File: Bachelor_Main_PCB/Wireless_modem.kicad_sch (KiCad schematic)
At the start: 57 parts, among them J10 JAE_SIM_Card_SF72S006, J12 M20-9990245, J18 CONMHF1-SMD-G-T, J19 CONMHF1-SMD-G-T, J20 CONMHF1-SMD-G-T, Q1 SSM3J358R,LF, Q10 NX3008NBKW, Q11 NX3008NBKW, Q5 NX3008NBKW, Q6 NX3008NBKW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

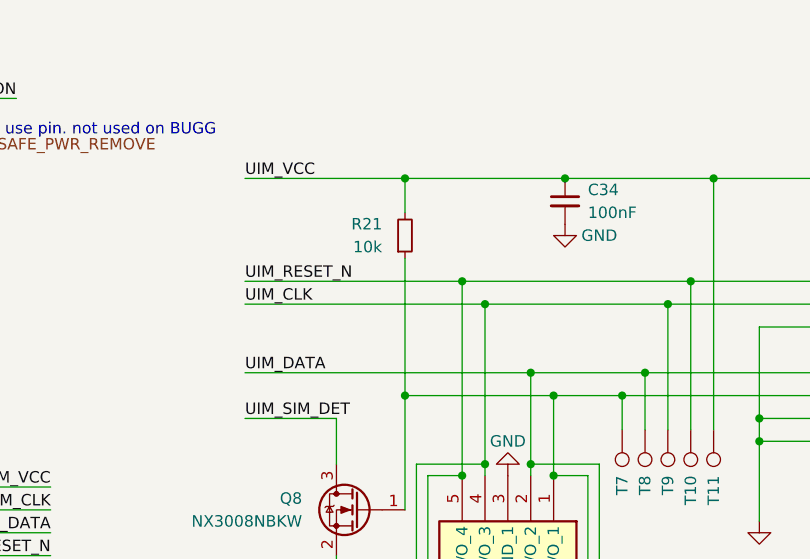
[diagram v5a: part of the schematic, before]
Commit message: add UIM_VCC to UIM_DATA pullout which is DNP
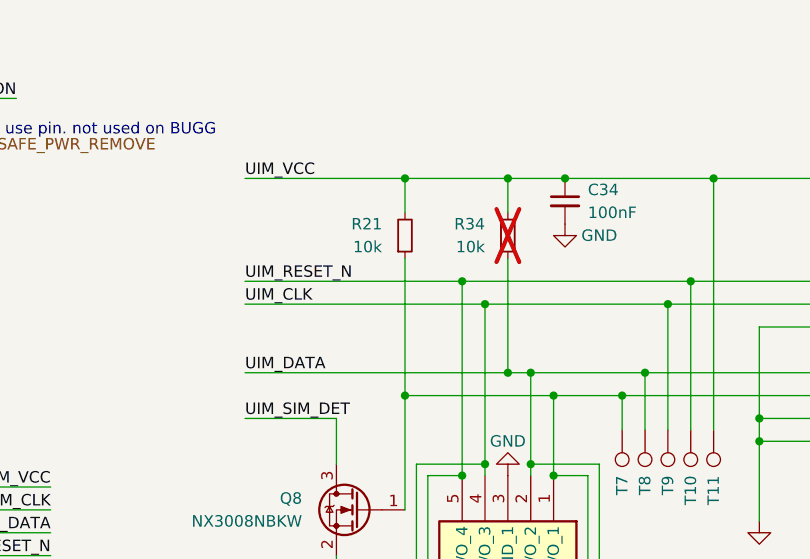
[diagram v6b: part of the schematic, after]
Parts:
- added R34: 10k, Resistor_SMD:R_0402_1005Metric, symbol Device:R_Small
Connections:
- net UIM_DATA: now also R34.1
- net UIM_VCC: now also R34.2
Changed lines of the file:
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@@
 	)
 	(junction
+		(at 209.55 33.02)
+		(diameter 0)
+		(color 0 0 0 0)
+	)
+	(junction
 		(at 38.1 102.87)
 		(diameter 0)
@@
 	)
 	(junction
+		(at 209.55 54.61)
+		(diameter 0)
+		(color 0 0 0 0)
+	)
+	(junction
 		(at 215.9 33.02)
 		(diameter 0)
@@
 	(wire
 		(pts
+			(xy 209.55 33.02) (xy 209.55 36.83)
+		)
+		(stroke
+			(width 0)
+			(type default)
+		)
+	)
+	(wire
+		(pts
 			(xy 128.27 181.61) (xy 135.89 181.61)
 		)
@@
 	(wire
 		(pts
+			(xy 209.55 41.91) (xy 209.55 54.61)
+		)
+		(stroke
+			(width 0)
+			(type default)
+		)
+	)
+	(wire
+		(pts
 			(xy 29.21 105.41) (xy 30.48 105.41)
 		)
@@
 	(wire
 		(pts
+			(xy 209.55 33.02) (xy 215.9 33.02)
+		)
+		(stroke
+			(width 0)
+			(type default)
+		)
+	)
+	(wire
+		(pts
 			(xy 193.04 107.95) (xy 193.04 109.22)
 		)
@@
 	(wire
 		(pts
-			(xy 198.12 33.02) (xy 215.9 33.02)
+			(xy 198.12 33.02) (xy 209.55 33.02)
 		)
 		(stroke
@@
 	(wire
 		(pts
-			(xy 180.34 54.61) (xy 212.09 54.61)
+			(xy 180.34 54.61) (xy 209.55 54.61)
 		)
 		(stroke
@@
 	(wire
 		(pts
+			(xy 209.55 54.61) (xy 212.09 54.61)
+		)
+		(stroke
+			(width 0)
+			(type default)
+		)
+	)
+	(wire
+		(pts
 			(xy 52.07 100.33) (xy 62.23 100.33)
 		)
@@
 					(unit 1)
 				)
+			)
+		)
+	)
+	(symbol
+		(lib_id "Device:R_Small")
+		(at 209.55 39.37 0)
+		(mirror x)
+		(unit 1)
+		(exclude_from_sim no)
+		(in_bom yes)
+		(on_board yes)
+		(dnp yes)
+		(property "Reference" "R34"
+			(at 207.01 38.1 0)
+			(effects
+				(font
+					(size 1.27 1.27)
+				)
+				(justify right)
+			)
+		)
+		(property "Value" "10k"
+			(at 207.01 40.64 0)
+			(effects
+				(font
+					(size 1.27 1.27)
+				)
+				(justify right)
+			)
+		)
+		(property "Footprint" "Resistor_SMD:R_0402_1005Metric"
+			(at 209.55 39.37 0)
+			(effects
+				(font
+					(size 1.27 1.27)
+				)
+				(hide yes)
+			)
+		)
+		(property "Datasheet" "~"
+			(at 209.55 39.37 0)
+			(effects
+				(font
+					(size 1.27 1.27)
+				)
+				(hide yes)
+			)
+		)
+		(property "Description" ""
+			(at 209.55 39.37 0)
+			(effects
+				(font
+					(size 1.27 1.27)
+				)
+				(hide yes)
+			)
+		)
+		(property "Quantity" ""
+			(at 209.55 39.37 0)
+			(effects
+				(font
+					(size 1.27 1.27)
+				)
+				(hide yes)
+			)
+		)
+		(property "Digikey" ""
+			(at 209.55 39.37 0)
+			(effects
+				(font
+					(size 1.27 1.27)
+				)
+				(hide yes)
+			)
+		)
+		(property "MPN" ""
+			(at 209.55 39.37 0)
+			(effects
+				(font
+					(size 1.27 1.27)
+				)
+				(hide yes)
+			)
+		)
+		(property "Mouser" ""
+			(at 209.55 39.37 0)
+			(effects
+				(font
+					(size 1.27 1.27)
+				)
+				(hide yes)
+			)
+		)
+		(property "Farnell" ""
+			(at 209.55 39.37 0)
+			(effects
+				(font
+					(size 1.27 1.27)
+				)
+				(hide yes)
+			)
+		)
+		(property "Field-1" ""
+			(at 209.55 39.37 0)
+			(effects
+				(font
+					(size 1.27 1.27)
+				)
+				(hide yes)
+			)
+		)
+		(property "Field4" ""
+			(at 209.55 39.37 0)
+			(effects
+				(font
+					(size 1.27 1.27)
+				)
+				(hide yes)
+			)
+		)
+		(property "Field5" ""
+			(at 209.55 39.37 0)
+			(effects
+				(font
+					(size 1.27 1.27)
+				)
+				(hide yes)
+			)
+		)
+		(property "MANUFACTURER" ""
+			(at 209.55 39.37 0)
+			(effects
+				(font
+					(size 1.27 1.27)
+				)
+				(hide yes)
+			)
+		)
+		(pin "1"
+		)
+		(pin "2"
+		)
+		(instances
+			(project "Bachelor_Main_PCB"
+				(path "/3544d663-329e-4884-b753-28436ca187e8/0bbef2a3-1d79-4cf0-b531-d6abf690b331"
+					(reference "R34")
+					(unit 1)
+				)

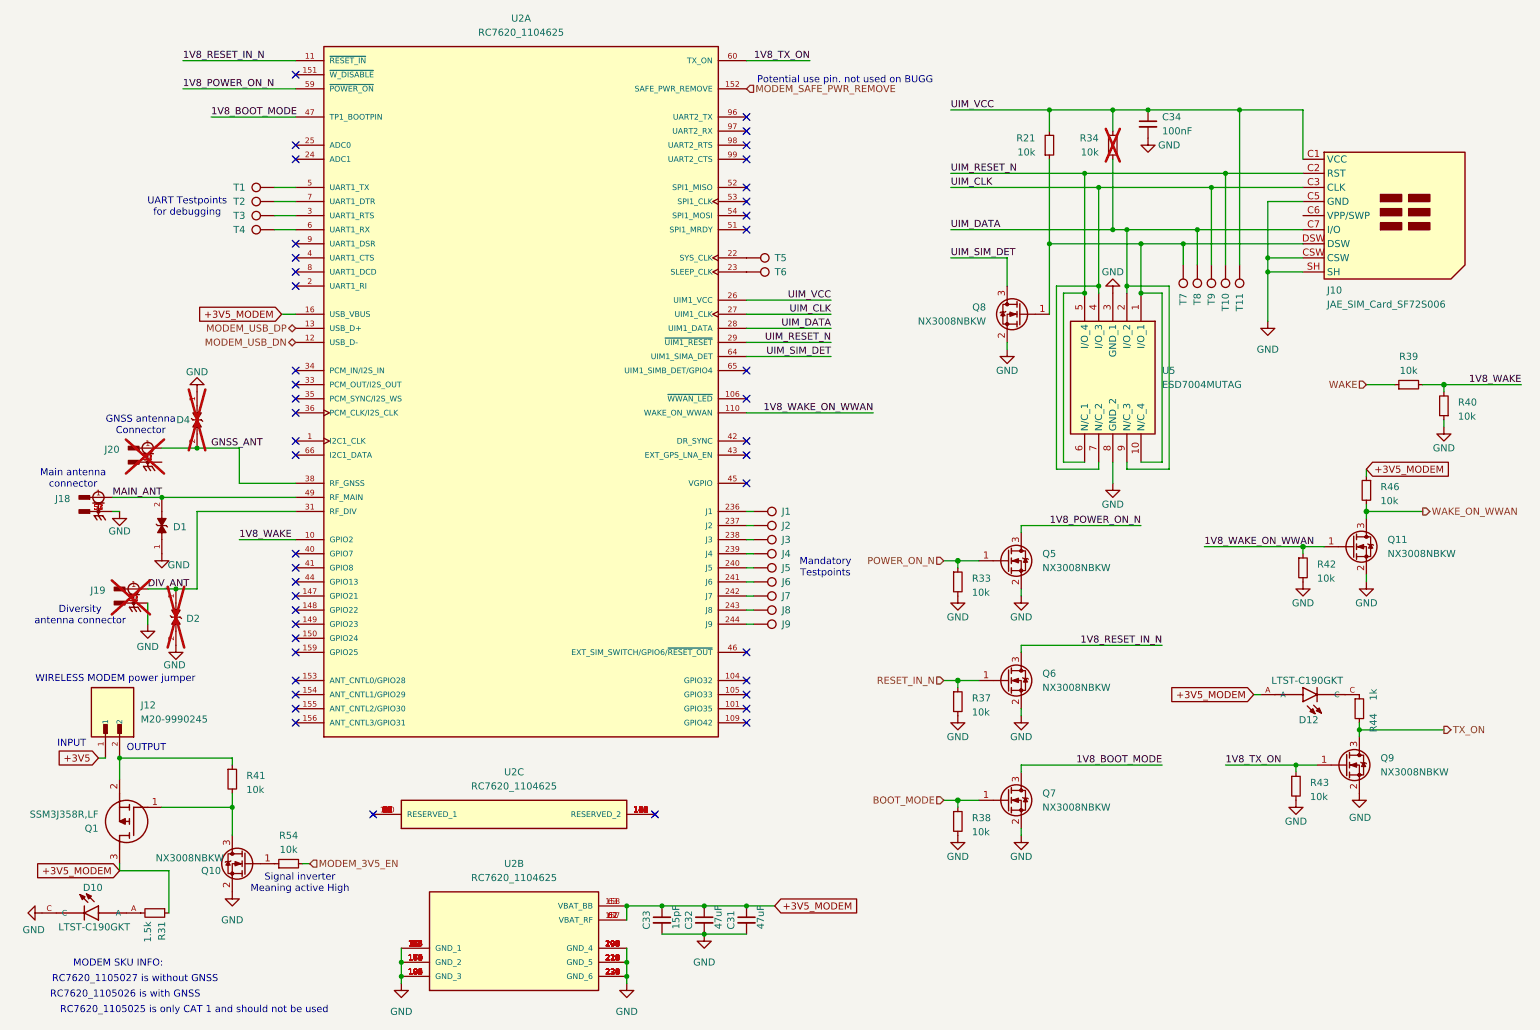
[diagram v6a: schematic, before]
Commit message: Updated the "Part-no" field in the symbol field table for all components
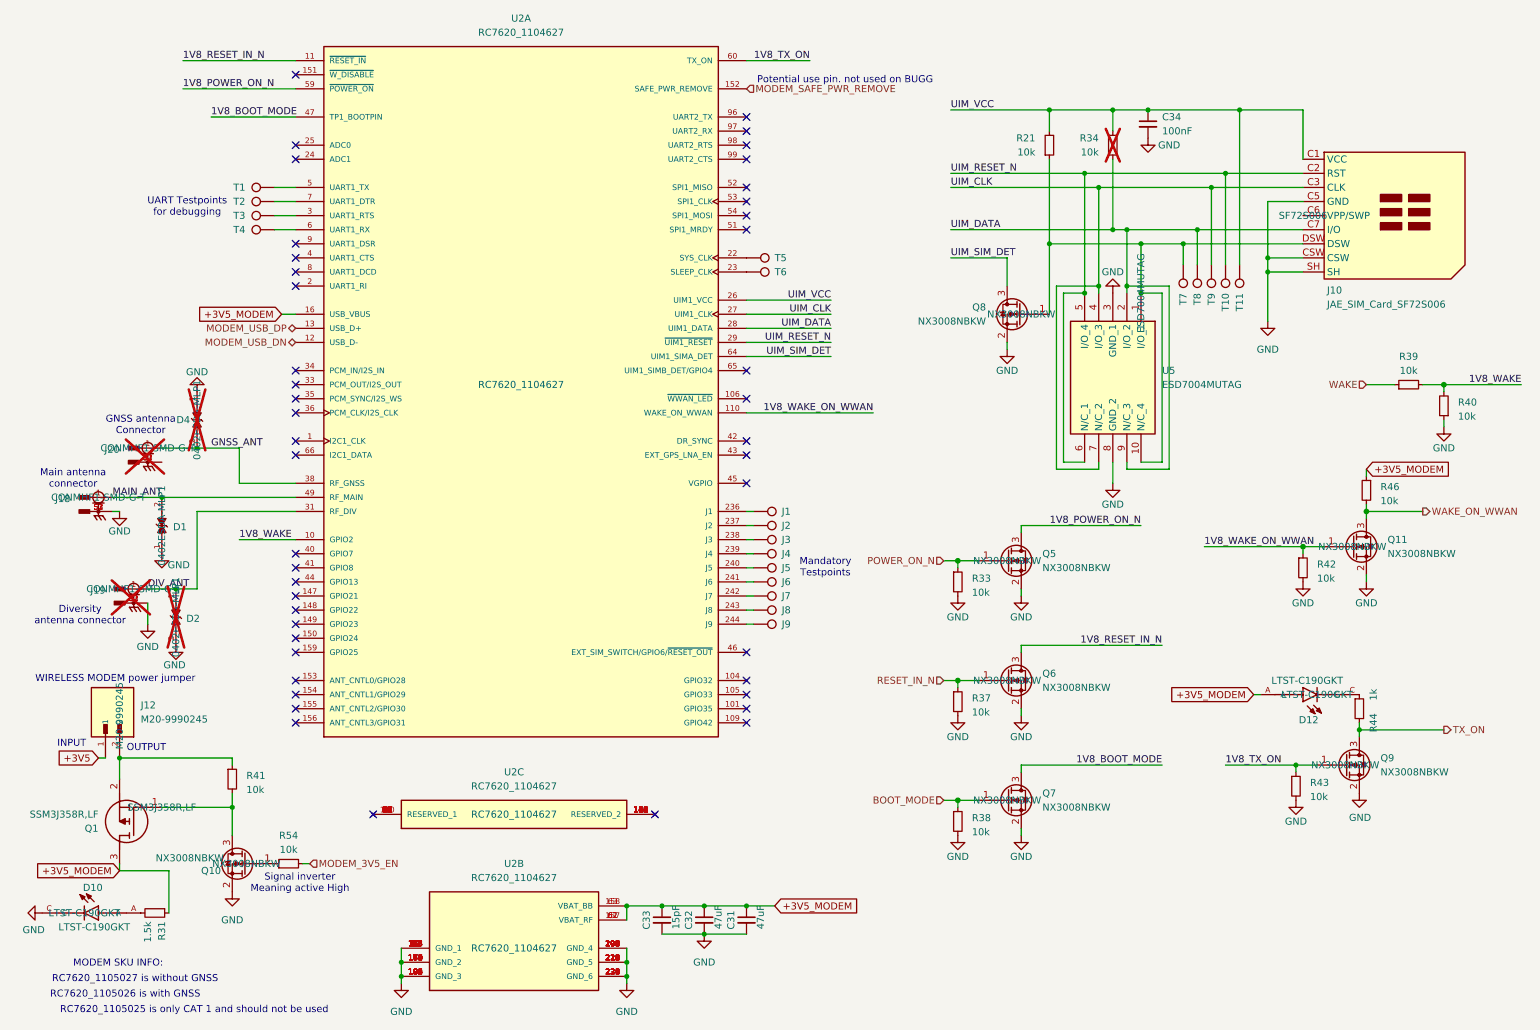
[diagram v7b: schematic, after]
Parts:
- C34: footprint Capacitor_SMD:C_0402_1005Metric -> Capacitor_SMD:C_0603_1608Metric
- D1, D2, D4: Part-no (none) -> 0402ESDA-MLP1
- D10, D12: Part-no (none) -> LTST-C190GKT
- J10: Part-no (none) -> SF72S006
- J12: Part-no (none) -> M20-9990245
- J18, J19, J20: Part-no (none) -> CONMHF1-SMD-G-T
- Q1: Part-no (none) -> SSM3J358R,LF
- Q10, Q11, Q5, Q6, Q7, Q8, Q9: Part-no (none) -> NX3008NBKW
- U2: value RC7620_1104625 -> RC7620_1104627; Check_prices https://www.snapeda.com/parts/RC7620_1104625/Sierra+Wireles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 -> https://www.snapeda.com/parts/RC7620_1104627/Sierra+Wireles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; MP RC7620_1104625 -> RC7620_1104627; Part-no (none) -> RC7620_1104627; SNAPEDA_PN RC7620_1104625 -> RC7620_1104627; SnapEDA_Link https://www.snapeda.com/parts/RC7620_1104625/Sierra+Wireles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 -> https://www.snapeda.com/parts/RC7620_1104627/Sierra+Wireles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
- U5: Part-no (none) -> ESD7004MUTAG
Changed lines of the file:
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@@
 			)
 		)
+		(property "Part-no" "CONMHF1-SMD-G-T"
+			(at 33.02 119.38 0)
+			(effects
+				(font
+					(size 1.27 1.27)
+				)
+			)
+		)
 		(pin "S1"
 		)
@@
 			)
 		)
+		(property "Part-no" "M20-9990245"
+			(at 30.48 142.24 0)
+			(effects
+				(font
+					(size 1.27 1.27)
+				)
+			)
+		)
 		(pin "2"
 		)
@@
 			)
 		)
+		(property "Part-no" "LTST-C190GKT"
+			(at 24.13 177.8 0)
+			(effects
+				(font
+					(size 1.27 1.27)
+				)
+			)
+		)
 		(pin "A"
 		)
@@
 			)
 		)
+		(property "Part-no" "NX3008NBKW"
+			(at 190.5 114.3 0)
+			(effects
+				(font
+					(size 1.27 1.27)
+				)
+			)
+		)
 		(pin "1"
 		)
@@
 			)
 		)
-		(property "Value" "RC7620_1104625"
+		(property "Value" "RC7620_1104627"
 			(at 102.87 19.05 0)
 			(effects
@@
 			)
 		)
-		(property "Check_prices" "https://www.snapeda.com/parts/RC7620_1104625/Sierra+Wireless/view-part/?ref=eda"
+		(property "Check_prices" "https://www.snapeda.com/parts/RC7620_1104627/Sierra+Wireless/view-part/?ref=eda"
 			(at 102.87 82.55 0)
 			(effects
@@
 			)
 		)
-		(property "SnapEDA_Link" "https://www.snapeda.com/parts/RC7620_1104625/Sierra+Wireless/view-part/?ref=snap"
+		(property "SnapEDA_Link" "https://www.snapeda.com/parts/RC7620_1104627/Sierra+Wireless/view-part/?ref=snap"
 			(at 102.87 82.55 0)
 			(effects
@@
 			)
 		)
-		(property "MP" "RC7620_1104625"
+		(property "MP" "RC7620_1104627"
 			(at 102.87 82.55 0)
 			(effects
@@
 			)
 		)
-		(property "SNAPEDA_PN" "RC7620_1104625"
+		(property "SNAPEDA_PN" "RC7620_1104627"
 			(at 102.87 82.55 0)
 			(effects
@@
 			)
 		)
+		(property "Part-no" "RC7620_1104627"
+			(at 102.87 82.55 0)
+			(effects
+				(font
+					(size 1.27 1.27)
+				)
+			)
+		)
 		(pin "38"
 		)
@@
 			)
 		)
+		(property "Part-no" "0402ESDA-MLP1"
+			(at 38.1 107.95 0)
+			(effects
+				(font
+					(size 1.27 1.27)
+				)
+			)
+		)
 		(pin "2"
 		)
@@
 			)
 		)
+		(property "Part-no" "ESD7004MUTAG"
+			(at 214.63 66.04 0)
+			(effects
+				(font
+					(size 1.27 1.27)
+				)
+			)
+		)
 		(pin "6"
 		)
@@
 			)
 		)
+		(property "Part-no" "NX3008NBKW"
+			(at 252.73 111.76 0)
+			(effects
+				(font
+					(size 1.27 1.27)
+				)
+			)
+		)
 		(pin "1"
 		)
@@
 			)
 		)
+		(property "Part-no" "NX3008NBKW"
+			(at 190.5 135.89 0)
+			(effects
+				(font
+					(size 1.27 1.27)
+				)
+			)
+		)
 		(pin "1"
 		)
@@
 			)
 		)
-		(property "Value" "RC7620_1104625"
+		(property "Value" "RC7620_1104627"
 			(at 101.6 171.45 0)
 			(effects
@@
 			)
 		)
-		(property "Check_prices" "https://www.snapeda.com/parts/RC7620_1104625/Sierra+Wireless/view-part/?ref=eda"
+		(property "Check_prices" "https://www.snapeda.com/parts/RC7620_1104627/Sierra+Wireless/view-part/?ref=eda"
 			(at 101.6 184.15 0)
 			(effects
@@
 			)
 		)
-		(property "SnapEDA_Link" "https://www.snapeda.com/parts/RC7620_1104625/Sierra+Wireless/view-part/?ref=snap"
+		(property "SnapEDA_Link" "https://www.snapeda.com/parts/RC7620_1104627/Sierra+Wireless/view-part/?ref=snap"
 			(at 101.6 184.15 0)
 			(effects
@@
 			)
 		)
-		(property "MP" "RC7620_1104625"
+		(property "MP" "RC7620_1104627"
 			(at 101.6 184.15 0)
 			(effects
@@
 			)
 		)
-		(property "SNAPEDA_PN" "RC7620_1104625"
+		(property "SNAPEDA_PN" "RC7620_1104627"
 			(at 101.6 184.15 0)
 			(effects
@@
 			)
 		)
+		(property "Part-no" "RC7620_1104627"
+			(at 101.6 184.15 0)
+			(effects
+				(font
+					(size 1.27 1.27)
+				)
+			)
+		)
 		(pin "38"
 		)
@@
 			)
 		)
+		(property "Part-no" "CONMHF1-SMD-G-T"
+			(at 35.56 93.98 0)
+			(effects
+				(font
+					(size 1.27 1.27)
+				)
+			)
+		)
 		(pin "S1"
 		)
@@
 			)
 		)
+		(property "Part-no" "SF72S006"
+			(at 243.84 52.07 0)
+			(effects
+				(font
+					(size 1.27 1.27)
+				)
+			)
+		)
 		(pin "C6"
 		)
@@
 			)
 		)
+		(property "Part-no" "0402ESDA-MLP1"
+			(at 40.64 124.46 0)
+			(effects
+				(font
+					(size 1.27 1.27)
+				)
+			)
+		)
 		(pin "2"
 		)
@@
 			)
 		)
-		(property "Footprint" "Capacitor_SMD:C_0402_1005Metric"
+		(property "Footprint" "Capacitor_SMD:C_0603_1608Metric"
 			(at 215.9 35.56 0)
 			(effects
@@
 			)
 		)
+		(property "Part-no" "0402ESDA-MLP1"
+			(at 44.45 88.9 0)
+			(effects
+				(font
+					(size 1.27 1.27)
+				)
+			)
+		)
 		(pin "2"
 		)
@@
 			)
 		)
+		(property "Part-no" "NX3008NBKW"
+			(at 193.04 69.85 0)
+			(effects
+				(font
+					(size 1.27 1.27)
+				)
+			)
+		)
 		(pin "1"
 		)
@@
 			)
 		)
+		(property "Part-no" "NX3008NBKW"
+			(at 53.34 168.91 0)
+			(effects
+				(font
+					(size 1.27 1.27)
+				)
+			)
+		)
 		(pin "1"
 		)
@@
 			)
 		)
+		(property "Part-no" "SSM3J358R,LF"
+			(at 38.1 158.75 0)
+			(effects
+				(font
+					(size 1.27 1.27)
+				)
+			)
+		)
 		(pin "3"
 		)
@@
 			)
 		)
+		(property "Part-no" "NX3008NBKW"
+			(at 251.46 151.13 0)
+			(effects
+				(font
+					(size 1.27 1.27)
+				)
+			)
+		)
 		(pin "1"
 		)
@@
 			)
 		)
+		(property "Part-no" "CONMHF1-SMD-G-T"
+			(at 26.67 102.87 0)
+			(effects
+				(font
+					(size 1.27 1.27)
+				)
+			)
+		)
 		(pin "S1"
 		)
@@
 			)
 		)
+		(property "Part-no" "LTST-C190GKT"
+			(at 246.38 138.43 0)
+			(effects
+				(font
+					(size 1.27 1.27)
+				)
+			)
+		)
 		(pin "A"
 		)
@@
 			)
 		)
+		(property "Part-no" "NX3008NBKW"
+			(at 190.5 157.48 0)
+			(effects
+				(font
+					(size 1.27 1.27)
+				)
+			)
+		)
 		(pin "1"
 		)
@@
 			)
 		)
-		(property "Value" "RC7620_1104625"
+		(property "Value" "RC7620_1104627"
 			(at 101.6 154.94 0)
 			(effects
@@
 			)
 		)
-		(property "Check_prices" "https://www.snapeda.com/parts/RC7620_1104625/Sierra+Wireless/view-part/?ref=eda"
+		(property "Check_prices" "https://www.snapeda.com/parts/RC7620_1104627/Sierra+Wireless/view-part/?ref=eda"
 			(at 101.6 160.02 0)
 			(effects
@@
 			)
 		)
-		(property "SnapEDA_Link" "https://www.snapeda.com/parts/RC7620_1104625/Sierra+Wireless/view-part/?ref=snap"
+		(property "SnapEDA_Link" "https://www.snapeda.com/parts/RC7620_1104627/Sierra+Wireless/view-part/?ref=snap"
 			(at 101.6 160.02 0)
 			(effects
@@
 			)
 		)
-		(property "MP" "RC7620_1104625"
+		(property "MP" "RC7620_1104627"
 			(at 101.6 160.02 0)
 			(effects
@@
 			)
 		)
-		(property "SNAPEDA_PN" "RC7620_1104625"
+		(property "SNAPEDA_PN" "RC7620_1104627"
 			(at 101.6 160.02 0)
 			(effects
@@
 			)
 		)
+		(property "Part-no" "RC7620_1104627"
+			(at 101.6 160.02 0)
+			(effects
+				(font
+					(size 1.27 1.27)
+				)
+			)
+		)

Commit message: All resistors and capacitors correct footprints
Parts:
- R21, R31, R33, R34, R37, R38, R39, R40, R41, R42, R43, R44, R46, R54: footprint Resistor_SMD:R_0402_1005Metric -> Resistor_SMD:R_0603_1608Metric
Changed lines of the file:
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@@
 			)
 		)
-		(property "Footprint" "Resistor_SMD:R_0402_1005Metric"
+		(property "Footprint" "Resistor_SMD:R_0603_1608Metric"
 			(at 255.27 101.6 0)
 			(effects
@@
 			)
 		)
-		(property "Footprint" "Resistor_SMD:R_0402_1005Metric"
+		(property "Footprint" "Resistor_SMD:R_0603_1608Metric"
 			(at 181.61 161.29 0)
 			(effects
@@
 			)
 		)
-		(property "Footprint" "Resistor_SMD:R_0402_1005Metric"
+		(property "Footprint" "Resistor_SMD:R_0603_1608Metric"
 			(at 243.84 115.57 0)
 			(effects
@@
 			)
 		)
-		(property "Footprint" "Resistor_SMD:R_0402_1005Metric"
+		(property "Footprint" "Resistor_SMD:R_0603_1608Metric"
 			(at 36.83 177.8 0)
 			(effects
@@
 			)
 		)
-		(property "Footprint" "Resistor_SMD:R_0402_1005Metric"
+		(property "Footprint" "Resistor_SMD:R_0603_1608Metric"
 			(at 181.61 139.7 0)
 			(effects
@@
 			)
 		)
-		(property "Footprint" "Resistor_SMD:R_0402_1005Metric"
+		(property "Footprint" "Resistor_SMD:R_0603_1608Metric"
 			(at 50.8 153.67 0)
 			(effects
@@
 			)
 		)
-		(property "Footprint" "Resistor_SMD:R_0402_1005Metric"
+		(property "Footprint" "Resistor_SMD:R_0603_1608Metric"
 			(at 269.24 86.36 0)
 			(effects
@@
 			)
 		)
-		(property "Footprint" "Resistor_SMD:R_0402_1005Metric"
+		(property "Footprint" "Resistor_SMD:R_0603_1608Metric"
 			(at 262.89 82.55 0)
 			(effects
@@
 			)
 		)
-		(property "Footprint" "Resistor_SMD:R_0402_1005Metric"
+		(property "Footprint" "Resistor_SMD:R_0603_1608Metric"
 			(at 254 140.97 0)
 			(effects
@@
 			)
 		)
-		(property "Footprint" "Resistor_SMD:R_0402_1005Metric"
+		(property "Footprint" "Resistor_SMD:R_0603_1608Metric"
 			(at 242.57 154.94 0)
 			(effects
@@
 			)
 		)
-		(property "Footprint" "Resistor_SMD:R_0402_1005Metric"
+		(property "Footprint" "Resistor_SMD:R_0603_1608Metric"
 			(at 198.12 39.37 0)
 			(effects
@@
 			)
 		)
-		(property "Footprint" "Resistor_SMD:R_0402_1005Metric"
+		(property "Footprint" "Resistor_SMD:R_0603_1608Metric"
 			(at 209.55 39.37 0)
 			(effects
@@
 			)
 		)
-		(property "Footprint" "Resistor_SMD:R_0402_1005Metric"
+		(property "Footprint" "Resistor_SMD:R_0603_1608Metric"
 			(at 181.61 118.11 0)
 			(effects
@@
 			)
 		)
-		(property "Footprint" "Resistor_SMD:R_0402_1005Metric"
+		(property "Footprint" "Resistor_SMD:R_0603_1608Metric"
 			(at 60.96 168.91 0)
 			(effects
